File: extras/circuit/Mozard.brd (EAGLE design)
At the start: 94 x 71.1 mm, 43 parts, among them J4 Headphone/Line Out, U2 LM386

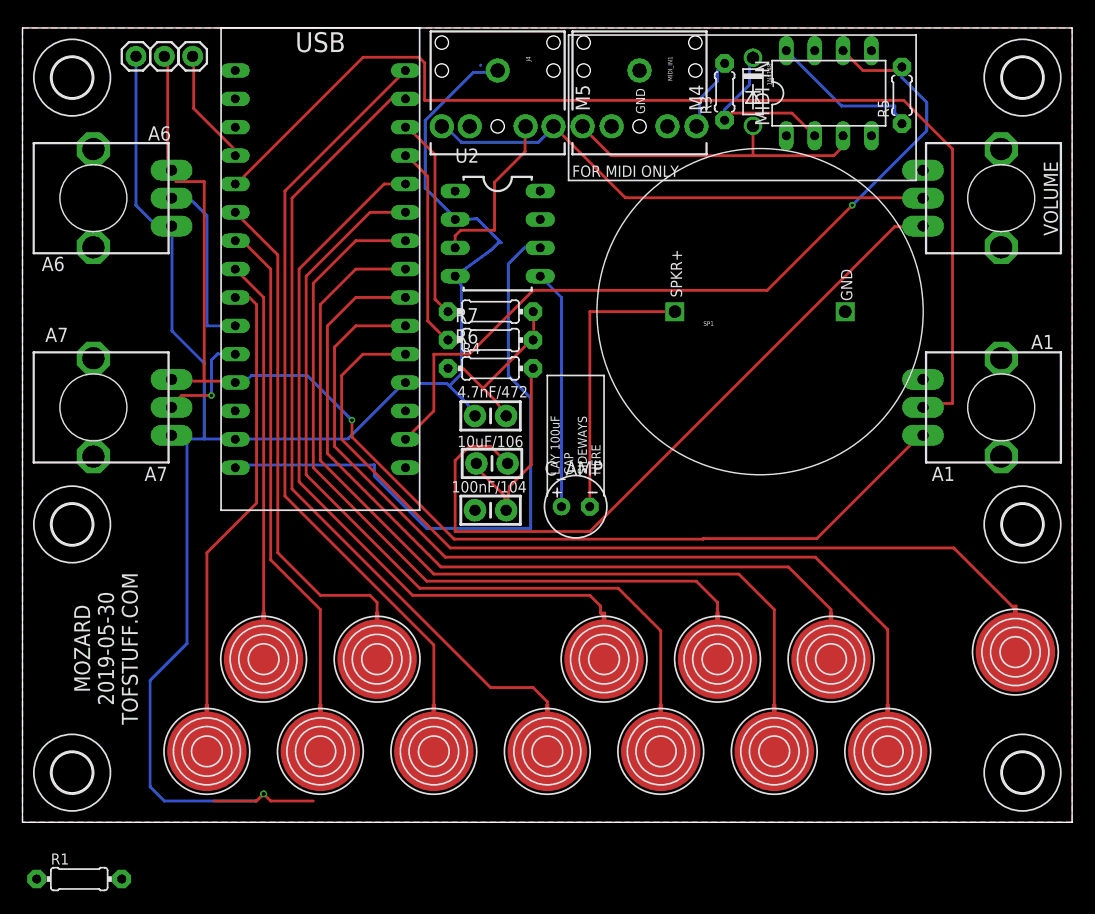
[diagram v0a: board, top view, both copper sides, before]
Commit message: Added MIDI
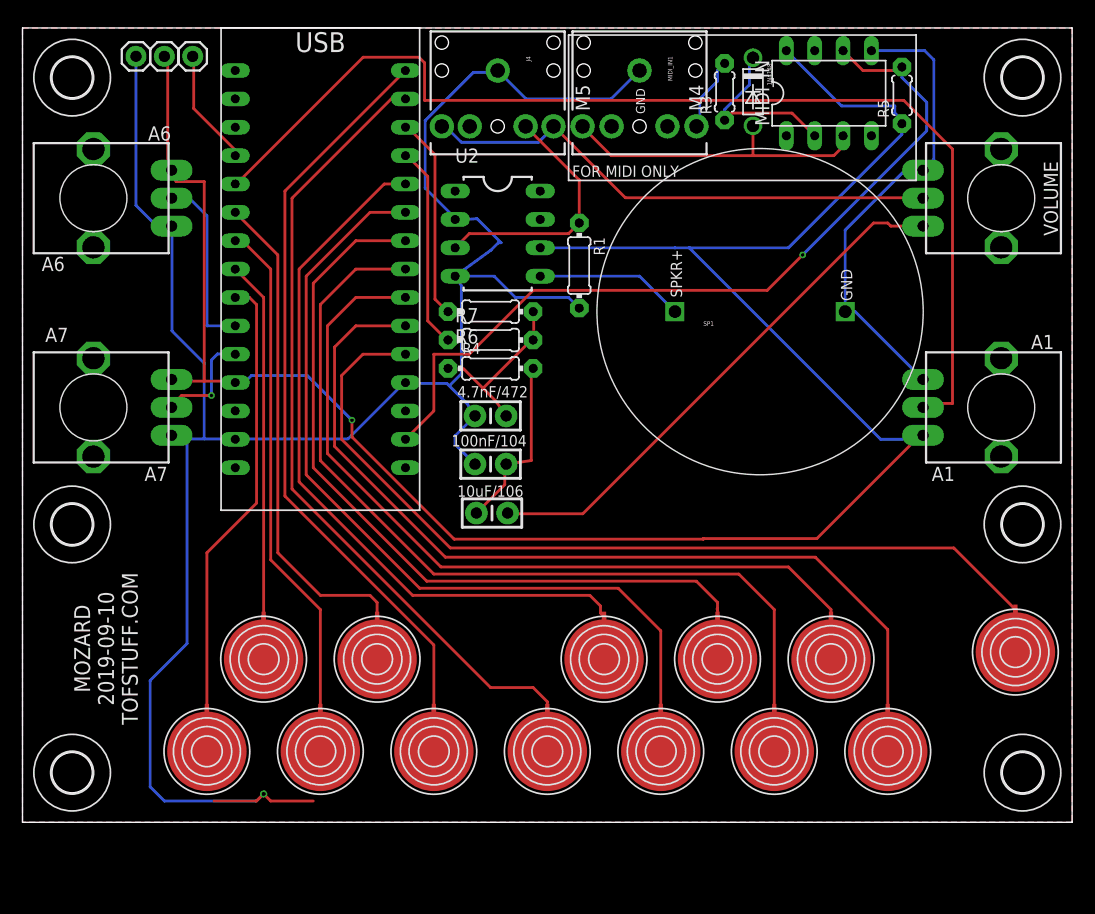
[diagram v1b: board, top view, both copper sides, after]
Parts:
- removed C_AMP: 100uF, TOF:E2,5-6
- moved R1 70.9 mm to (49.8, 49.8), turned to 270 degrees
- moved C2 4.45 mm to (42.0, 27.7)
- moved C4 4.13 mm to (41.9, 32.1)
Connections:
- removed net 5V: MIDI_IN.8, R5.1
- removed net N$7: C_AMP.+, U2.5
- removed net V+: U$1.RAW, U2.6
- net N$1: now also U2.5; no longer C_AMP.-
- net VCC: now also MIDI_IN.8, R5.1, U2.6
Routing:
- net VCC: track 110.9 -> 190.3 mm
- net GND: track 160.3 -> 235.4 mm
- net V+: track 57.4 -> 0.00 mm
- net N$7: track 21.4 -> 0.00 mm
- net N$2: track 65.4 -> 48.1 mm
- net 5V: track 13.6 -> 0.00 mm
- net N$1: track 25.1 -> 13.4 mm
- net N$6: track 15.2 -> 22.7 mm
- net N$4: track 19.0 -> 16.2 mm
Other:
- board text added: "MOZARD 2019-09-10 TOFSTUFF.COM"
- board text removed: "LAY 100uF CAP SIDEWAYS HERE"
- board text removed: "MOZARD 2019-05-30 TOFSTUFF.COM"

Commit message: New board + poly
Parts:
- removed JP6: A0, TOF:1X01_SIDE_NAME
- added U$15: PCB-TOUCHPAD-1-PIN, TOF:PCB-TOUCHPAD-1-PIN
- moved JP5 1.27 mm to (14.0, 68.6)
- moved JP2 1.27 mm to (11.4, 68.6)
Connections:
- net N$1 renamed LM386_OUTPUT
- removed net A0: JP6.1, U$1.A0
- new net N$3: U$1.A0, U$15.1
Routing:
- net N$3: track 0.00 -> 52.3 mm
- net A0: track 10.4 -> 0.00 mm
- net GND: track 235.4 -> 237.3 mm
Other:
- board text added: "MOZARD 2019-09-19 TOFSTUFF.COM"
- board text removed: "MOZARD 2019-09-10 TOFSTUFF.COM"
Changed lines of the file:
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@@
 <?xml version="1.0" encoding="utf-8"?>
 <!DOCTYPE eagle SYSTEM "eagle.dtd">
-<eagle version="9.3.1">
+<eagle version="9.5.0">
 <drawing>
 <settings>
@@
 <setting verticaltext="up"/>
 </settings>
-<grid distance="0.1" unitdist="inch" unit="inch" style="lines" multiple="1" display="yes" altdistance="0.0125" altunitdist="inch" altunit="inch"/>
+<grid distance="0.1" unitdist="inch" unit="inch" style="lines" multiple="1" display="yes" altdistance="0.05" altunitdist="inch" altunit="inch"/>
 <layers>
 <layer number="1" name="Top" color="4" fill="1" visible="yes" active="yes"/>
@@
 <wire x1="93.98" y1="71.12" x2="0" y2="71.12" width="0.0254" layer="20"/>
 <wire x1="0" y1="71.12" x2="0" y2="0" width="0.027940625" layer="20"/>
-<text x="4.6309875" y="15.5529875" size="1.4224" layer="21" font="vector" rot="R270" align="bottom-center">MOZARD
-2019-09-10
-TOFSTUFF.COM</text>
+<text x="55.5670125" y="22.4109875" size="1.4224" layer="28" font="vector" rot="MR0" align="bottom-center">MOZARD 2019-09-19 TOFSTUFF.COM</text>
 <text x="74.295" y="46.6725" size="1.016" layer="21" rot="R90">GND</text>
 <text x="59.055" y="46.99" size="1.016" layer="21" rot="R90">SPKR+</text>
@@
 <attribute name="VALUE" x="63.8175" y="45.72" size="0.762" layer="27"/>
 </element>
-<element name="JP2" library="TOF" package="1X01_SIDE_NAME" value="GND" x="10.16" y="68.58" smashed="yes" rot="R270">
-<attribute name="VALUE" x="9.4488" y="66.7512" size="1.27" layer="27" rot="R270"/>
-</element>
-<element name="JP5" library="TOF" package="1X01_SIDE_NAME" value="5V" x="12.7" y="68.58" smashed="yes" rot="R270">
-<attribute name="VALUE" x="11.9888" y="66.7512" size="1.27" layer="27" rot="R270"/>
-</element>
-<element name="JP6" library="TOF" package="1X01_SIDE_NAME" value="A0" x="15.24" y="68.58" smashed="yes" rot="R270">
-<attribute name="VALUE" x="14.5288" y="66.7512" size="1.27" layer="27" rot="R270"/>
+<element name="JP2" library="TOF" package="1X01_SIDE_NAME" value="GND" x="11.43" y="68.58" smashed="yes" rot="R270">
+<attribute name="VALUE" x="10.7188" y="66.7512" size="1.27" layer="27" rot="R270"/>
+</element>
+<element name="JP5" library="TOF" package="1X01_SIDE_NAME" value="5V" x="13.97" y="68.58" smashed="yes" rot="R270">
+<attribute name="VALUE" x="13.2588" y="66.7512" size="1.27" layer="27" rot="R270"/>
 </element>
 <element name="A1" library="TOF" package="ALPS_POT" value="A1" x="87.63" y="37.1475" smashed="yes" rot="R180">
@@
 <attribute name="VALUE" x="49.3649" y="51.4731" size="0.9906" layer="27" ratio="12" rot="R270"/>
 </element>
+<element name="U$15" library="TOF" package="PCB-TOUCHPAD-1-PIN" value="PCB-TOUCHPAD-1-PIN" x="5.08" y="15.24" smashed="yes" rot="R270"/>
 </elements>
 <signals>
@@
 <wire x1="40.6908" y1="54.0512" x2="39.8526" y2="53.975" width="0.254" layer="16"/>
 <wire x1="37.9984" y1="39.2938" x2="34.3281" y2="39.2938" width="0.254" layer="16"/>
-<wire x1="38.2143" y1="39.0779" x2="37.9984" y2="39.2938" width="0.254" layer="16"/>
-<wire x1="39.824025" y1="37.468175" x2="38.2143" y2="39.0779" width="0.254" layer="16"/>
+<wire x1="39.824025" y1="37.468175" x2="38.69055" y2="38.60165" width="0.254" layer="16"/>
+<wire x1="38.69055" y1="38.60165" x2="37.9984" y2="39.2938" width="0.254" layer="16"/>
 <wire x1="34.3281" y1="39.2938" x2="34.29" y2="39.37" width="0.254" layer="16"/>
 <wire x1="39.824025" y1="37.468175" x2="40.513" y2="36.3855" width="0.254" layer="16"/>
-<wire x1="39.2938" y1="40.1574" x2="39.2938" y2="48.0568" width="0.254" layer="16"/>
-<wire x1="38.2143" y1="39.0779" x2="39.2938" y2="40.1574" width="0.254" layer="16"/>
-<wire x1="39.2938" y1="48.0568" x2="38.735" y2="48.895" width="0.254" layer="16"/>
+<wire x1="40.8813" y1="40.7924" x2="40.8813" y2="45.67555" width="0.254" layer="16"/>
+<wire x1="38.69055" y1="38.60165" x2="40.8813" y2="40.7924" width="0.254" layer="16"/>
+<wire x1="40.8813" y1="45.67555" x2="38.735" y2="48.895" width="0.254" layer="16"/>
 <wire x1="40.3733" y1="67.1449" x2="42.5323" y2="67.1449" width="0.254" layer="16"/>
 <wire x1="36.0553" y1="62.8269" x2="40.3733" y2="67.1449" width="0.254" layer="16"/>
@@
 <wire x1="16.2687" y1="34.3281" x2="16.2687" y2="41.1099" width="0.254" layer="16"/>
 <wire x1="13.3858" y1="53.3273" x2="13.35" y2="53.38" width="0.254" layer="16"/>
-<wire x1="10.16" y1="68.58" x2="10.16" y2="55.245" width="0.254" layer="16"/>
+<wire x1="11.43" y1="68.58" x2="10.16" y2="67.31" width="0.254" layer="16"/>
+<wire x1="10.16" y1="67.31" x2="10.16" y2="55.245" width="0.254" layer="16"/>
 <wire x1="12.0777" y1="53.3273" x2="13.3858" y2="53.3273" width="0.254" layer="16"/>
 <wire x1="10.16" y1="55.245" x2="12.0777" y2="53.3273" width="0.254" layer="16"/>
@@
 <wire x1="19" y1="39.5" x2="19.05" y2="39.37" width="0.254" layer="1"/>
 <wire x1="13.5" y1="39.5" x2="13.35" y2="39.6475" width="0.254" layer="1"/>
-<wire x1="13" y1="68.5" x2="13" y2="58.5" width="0.254" layer="1"/>
-<wire x1="13" y1="58.5" x2="13.35" y2="58.38" width="0.254" layer="1"/>
-<wire x1="13" y1="68.5" x2="12.7" y2="68.58" width="0.254" layer="1"/>
 <wire x1="16.27" y1="57.365" x2="16.27" y2="39.5" width="0.254" layer="1"/>
 <wire x1="13.750659375" y1="57.365" x2="16.27" y2="57.365" width="0.254" layer="1"/>
@@
 <wire x1="60.96" y1="25.4" x2="60.96" y2="25.3492" width="0.254" layer="1"/>
 <contactref element="U2" pad="6"/>
-<wire x1="46.355" y1="51.435" x2="58.42" y2="51.435" width="0.254" layer="16"/>
-<wire x1="58.42" y1="51.435" x2="59.69" y2="51.435" width="0.254" layer="16"/>
+<wire x1="46.355" y1="51.435" x2="59.69" y2="51.435" width="0.254" layer="16"/>
 <wire x1="59.69" y1="51.435" x2="76.835" y2="34.29" width="0.254" layer="16"/>
 <wire x1="76.835" y1="34.29" x2="80.2725" y2="34.29" width="0.254" layer="16"/>
@@
 <wire x1="68.58" y1="51.435" x2="78.74" y2="61.595" width="0.254" layer="16"/>
 <wire x1="78.74" y1="61.595" x2="78.74" y2="62.5475" width="0.254" layer="16"/>
+<wire x1="13.97" y1="68.58" x2="13.35" y2="67.96" width="0.254" layer="16"/>
+<wire x1="13.35" y1="67.96" x2="13.35" y2="58.38" width="0.254" layer="16"/>
 </signal>
 <signal name="D9(AUDIO3.9K)">
@@
 <wire x1="49.8475" y1="53.6575" x2="49.8475" y2="57.5075" width="0.254" layer="1"/>
 <wire x1="49.8475" y1="57.5075" x2="45.045" y2="62.31" width="0.254" layer="1"/>
-</signal>
-<signal name="A0">
-<contactref element="U$1" pad="A0"/>
-<contactref element="JP6" pad="1"/>
-<wire x1="18.9992" y1="60.2361" x2="18.9992" y2="59.8043" width="0.254" layer="1"/>
-<wire x1="15.3289" y1="63.9064" x2="18.9992" y2="60.2361" width="0.254" layer="1"/>
-<wire x1="15.3289" y1="68.4403" x2="15.3289" y2="63.9064" width="0.254" layer="1"/>
-<wire x1="18.9992" y1="59.8043" x2="19.05" y2="59.69" width="0.254" layer="1"/>
-<wire x1="15.3289" y1="68.4403" x2="15.24" y2="68.58" width="0.254" layer="1"/>
 </signal>
 <signal name="D11">
@@
 <wire x1="60.6425" y1="62.5475" x2="60.345" y2="62.31" width="0.254" layer="16"/>
 </signal>
-<signal name="N$1">
+<signal name="LM386_OUTPUT">
 <contactref element="U2" pad="5"/>
 <contactref element="SP1" pad="+"/>
 <wire x1="46.355" y1="48.895" x2="55.245" y2="48.895" width="0.254" layer="16"/>
 <wire x1="55.245" y1="48.895" x2="58.42" y2="45.72" width="0.254" layer="16"/>
+</signal>
+<signal name="N$3">
+<contactref element="U$15" pad="1"/>
+<contactref element="U$1" pad="A0"/>
+<wire x1="19.05" y1="59.69" x2="16.51" y2="59.69" width="0.254" layer="1"/>
+<wire x1="16.51" y1="59.69" x2="15.24" y2="60.96" width="0.254" layer="1"/>
+<wire x1="15.24" y1="60.96" x2="12.065" y2="60.96" width="0.254" layer="1"/>
+<wire x1="10.16" y1="59.055" x2="12.065" y2="60.96" width="0.254" layer="1"/>
+<wire x1="5.08" y1="19.05" x2="10.16" y2="24.13" width="0.254" layer="1"/>
+<wire x1="10.16" y1="24.13" x2="10.16" y2="59.055" width="0.254" layer="1"/>
 </signal>
 </signals>
@@
 </drawing>
 <compatibility>
-<note version="6.3" minversion="6.2.2" severity="warning">
-Since Version 6.2.2 text objects can contain more than one line,
-which will not be processed correctly with this version.
-</note>
 <note version="8.2" severity="warning">
 Since Version 8.2, EAGLE supports online libraries. The ids
